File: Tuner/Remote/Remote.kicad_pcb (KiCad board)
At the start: 2 copper layers, 96.8 x 99.3 mm, 100 parts, among them J1 Conn_01x05, J10 Conn_01x05, J11 Conn_01x04, J12 Conn_01x04, J13 Conn_01x01, J14 Conn_01x01, J15 Conn_01x02, J16 Conn_01x06, J17 Conn_01x02, J18 Conn_01x01, J19 Conn_01x01, J2 Conn_01x05, J20 Conn_01x01, J21 Conn_01x01, J22 Conn_01x01, J23 Conn_01x01, J24 Conn_01x02, J26 Conn_01x02, J27 Conn_01x02, J3 USB_B, J4 Conn_01x04, J5 Conn_01x20, J6 Conn_02x03_Odd_Even, J7 Conn_01x02, J8 Conn_01x06, J9 Conn_01x20, Q1 2N7000, Q2 2N7000, Q3 2N7000, Q4 2N7000, U1 LM1117-3.3, U2 STM32F103C8T6, U4 LM7805_TO220, Y1 8 MHz, Y2 Crystal

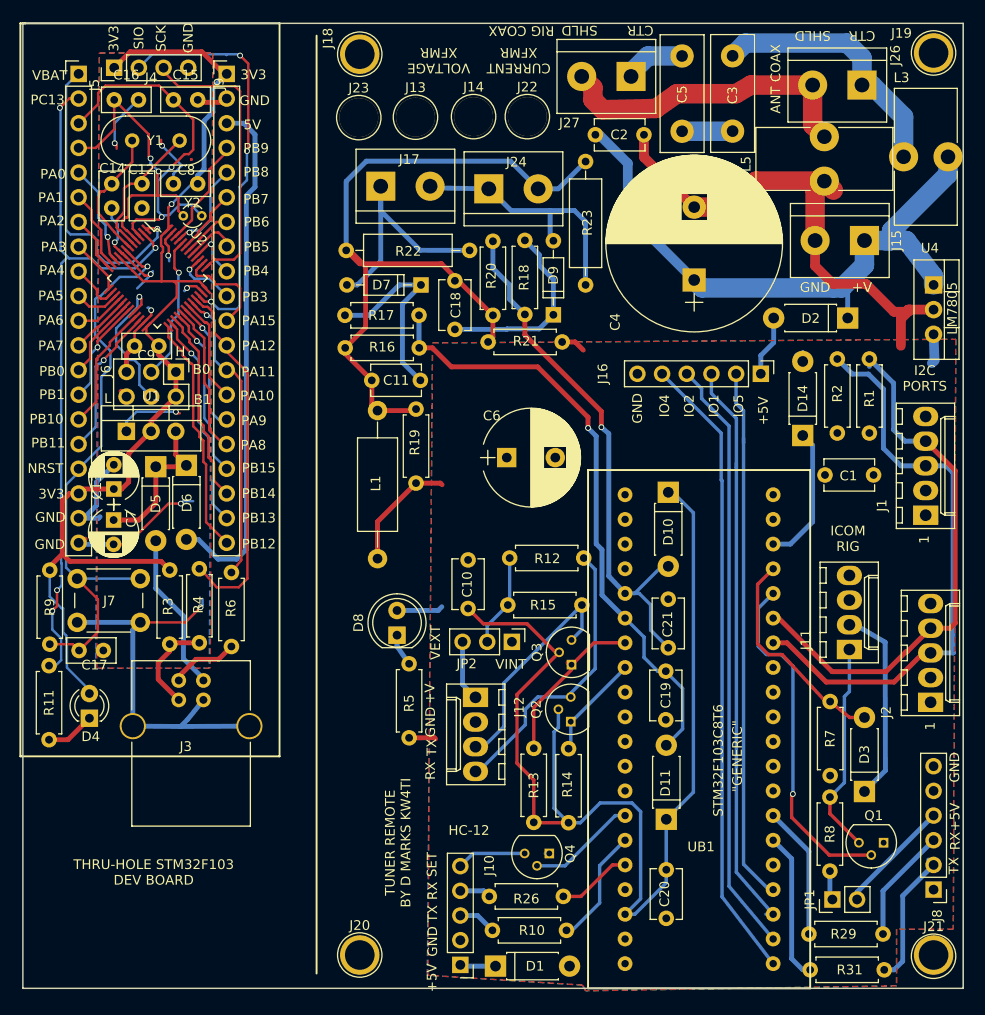
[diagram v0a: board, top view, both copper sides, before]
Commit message: JLCPCB order 09232018 - improved grounding - improved I2C cabling - NEO7M port - support for common mode chokes - relay board now has capacitors on all coils
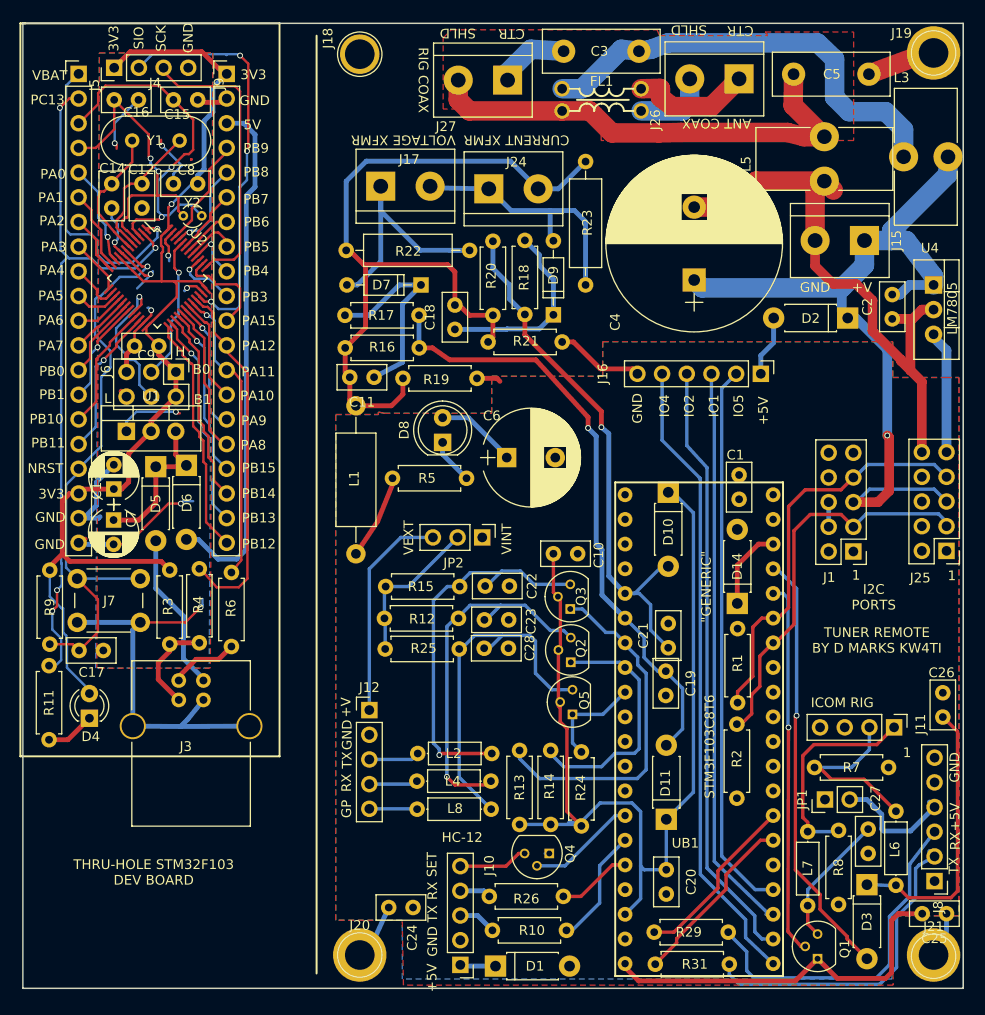
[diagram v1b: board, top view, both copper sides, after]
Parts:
- removed J13, J14, J22, J23: Conn_01x01, Connectors:1pin
- removed J2: Conn_01x05, Connectors_Molex:Molex_KK-6410-05_05x2.54mm_Straight
- added C22: 0.1 uF, Capacitors_THT:C_Disc_D5.0mm_W2.5mm_P2.50mm, F.Cu at (102.9, 86.9)
- added C23: 0.1 uF, Capacitors_THT:C_Disc_D5.0mm_W2.5mm_P2.50mm, F.Cu at (102.9, 90.3)
- added C24: 0.1 uF, Capacitors_THT:C_Disc_D5.0mm_W2.5mm_P2.50mm, F.Cu at (93.0, 120.0)
- added C25: 0.1 uF, Capacitors_THT:C_Disc_D5.0mm_W2.5mm_P2.50mm, F.Cu at (150.4, 120.6)
- added C26: 0.1 uF, Capacitors_THT:C_Disc_D5.0mm_W2.5mm_P2.50mm, F.Cu at (150.1, 97.9)
- added C27: 0.1 uF, Capacitors_THT:C_Disc_D5.0mm_W2.5mm_P2.50mm, F.Cu at (142.4, 111.9)
- added C28: 0.1 uF, Capacitors_THT:C_Disc_D5.0mm_W2.5mm_P2.50mm, F.Cu at (102.8, 93.3)
- added FL1: EMI_Filter_CommonMode, Remote:GenericCMCL, F.Cu at (114.9, 38.2)
- added J25: Conn_02x05_Odd_Even, Pin_Headers:Pin_Header_Straight_2x05_Pitch2.54mm, F.Cu at (150.4, 83.2)
- added L2: 100 uH, Inductors_THT:L_Axial_L5.3mm_D2.2mm_P7.62mm_Horizontal_Vishay_IM-1, F.Cu at (96.0, 104.1)
- added L4: 100 uH, Inductors_THT:L_Axial_L5.3mm_D2.2mm_P7.62mm_Horizontal_Vishay_IM-1, F.Cu at (95.9, 106.9)
- added L6: 100 uH, Inductors_THT:L_Axial_L5.3mm_D2.2mm_P7.62mm_Horizontal_Vishay_IM-1, F.Cu at (145.2, 117.7)
- added L7: 100 uH, Inductors_THT:L_Axial_L5.3mm_D2.2mm_P7.62mm_Horizontal_Vishay_IM-1, F.Cu at (136.1, 119.8)
- added L8: 100 uH, Inductors_THT:L_Axial_L5.3mm_D2.2mm_P7.62mm_Horizontal_Vishay_IM-1, F.Cu at (95.9, 109.8)
- added Q5: 2N7000, TO_SOT_Packages_THT:TO-92_Molded_Narrow, F.Cu at (111.9, 100.1)
- added R24: 10k, Resistors_THT:R_Axial_DIN0207_L6.3mm_D2.5mm_P7.62mm_Horizontal, F.Cu at (112.9, 103.9)
- added R25: 10k, Resistors_THT:R_Axial_DIN0207_L6.3mm_D2.5mm_P7.62mm_Horizontal, F.Cu at (92.7, 93.3)
- C1, C10, C11, C18, C19, C2, C20, C21: footprint Capacitors_THT:C_Disc_D5.1mm_W3.2mm_P5.00mm -> Capacitors_THT:C_Disc_D5.0mm_W2.5mm_P2.50mm
- J1: value Conn_01x05 -> Conn_02x05_Odd_Even; footprint Connectors_Molex:Molex_KK-6410-05_05x2.54mm_Straight -> Pin_Headers:Pin_Header_Straight_2x05_Pitch2.54mm
- J11: footprint Connectors_Molex:Molex_KK-6410-04_04x2.54mm_Straight -> Pin_Headers:Pin_Header_Straight_1x04_Pitch2.54mm
- J12: value Conn_01x04 -> Conn_01x05; footprint Connectors_Molex:Molex_KK-6410-04_04x2.54mm_Straight -> Pin_Headers:Pin_Header_Straight_1x05_Pitch2.54mm
- R12, R13, R14, R15: value 1k -> 10k
- moved R2 39.0 mm to (128.9, 108.7)
- moved C2 31.8 mm to (144.8, 59.4), turned to 90 degrees
- moved R1 24.3 mm to (128.9, 91.3), turned to 270 degrees
- moved D8 20.4 mm to (98.6, 72.1)
- moved C5 20.1 mm to (142.4, 34.2), turned to 180 degrees
- moved R5 20.0 mm to (101.0, 75.8), turned to 180 degrees
- moved D14 18.6 mm to (128.9, 88.7)
- moved R31 16.0 mm to (128.1, 125.8)
- moved R29 15.9 mm to (128.0, 122.5)
- moved R12 14.3 mm to (100.2, 90.2)
- moved Q1 13.7 mm to (137.2, 125.2), turned to 90 degrees
- moved R15 12.7 mm to (100.3, 86.9)
- moved J27 12.7 mm to (105.3, 34.8)
- moved J26 12.7 mm to (129.1, 34.7)
- moved R19 12.5 mm to (102.1, 65.5), turned to 180 degrees
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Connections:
- C2 pad 2: Net-(C2-Pad2) -> UPWR
- C4 pad 1: Net-(C2-Pad2) -> UPWR
- C5 pad 1: Net-(C3-Pad2) -> Net-(C5-Pad1)
- D2 pad 1: Net-(C2-Pad2) -> UPWR
- D3 pad 1: Net-(D3-Pad1) -> Net-(C26-Pad2)
- J1 pad 4: I2CSDA -> GND
- J1 pad 5: (no net) -> UPWR
- J11 pad 2: Net-(D3-Pad1) -> Net-(J11-Pad2)
- J15 pad 1: Net-(C2-Pad2) -> UPWR
- J19 pad 1: (no net) -> Net-(C5-Pad1)
- J20 pad 1: (no net) -> Net-(C24-Pad1)
- J21 pad 1: (no net) -> Net-(C25-Pad1)
- J26 pad 1: Net-(C3-Pad1) -> Net-(FL1-Pad1)
- J26 pad 2: SHIELD -> Net-(FL1-Pad3)
- J27 pad 1: Net-(C5-Pad2) -> Net-(C3-Pad2)
- J27 pad 2: SHIELD -> Net-(C5-Pad2)
- L3 pad 2: Net-(C2-Pad2) -> UPWR
- L5 pad 1: SHIELD -> Net-(C5-Pad2)
- Q1 pad 3: Net-(J11-Pad1) -> Net-(C27-Pad1)
- Q2 pad 3: Net-(J12-Pad4) -> Net-(C23-Pad1)
- Q3 pad 3: Net-(J12-Pad3) -> Net-(C22-Pad1)
- R12 pad 1: Net-(J12-Pad4) -> Net-(C23-Pad1)
- R15 pad 1: Net-(J12-Pad3) -> Net-(C22-Pad1)
- R7 pad 2: Net-(D3-Pad2) -> Net-(J11-Pad2)
- U4 pad 1: Net-(C2-Pad2) -> UPWR
- UB1 pad 14: (no net) -> Net-(Q5-Pad1)
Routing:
- net UPWR: track 0.00 -> 86.5 mm, vias 0 -> 1
- net Net-(C2-Pad2): track 70.5 -> 0.00 mm
- net GND: track 72.8 -> 123.0 mm
- net Net-(C5-Pad2): track 7.92 -> 48.9 mm
- net Net-(C22-Pad1): track 0.00 -> 40.2 mm, vias 0 -> 1
- net Net-(C23-Pad1): track 0.00 -> 38.7 mm, vias 0 -> 1
- net Net-(C28-Pad1): track 0.00 -> 36.7 mm
- net SHIELD: track 32.8 -> 0.00 mm
- net Net-(C26-Pad2): track 0.00 -> 28.8 mm
- net Net-(J12-Pad4): track 31.6 -> 5.02 mm
- net Net-(J8-Pad3): track 11.8 -> 35.7 mm
- net Net-(D3-Pad2): track 22.6 -> 44.6 mm, vias 0 -> 1
- net Net-(D3-Pad1): track 21.3 -> 0.00 mm
- net I2CSCL: track 60.3 -> 41.0 mm
- net Net-(J8-Pad2): track 14.2 -> 33.4 mm
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- added copper zone on F.Cu, net Net-(C5-Pad2)
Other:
- board text added: "GP"

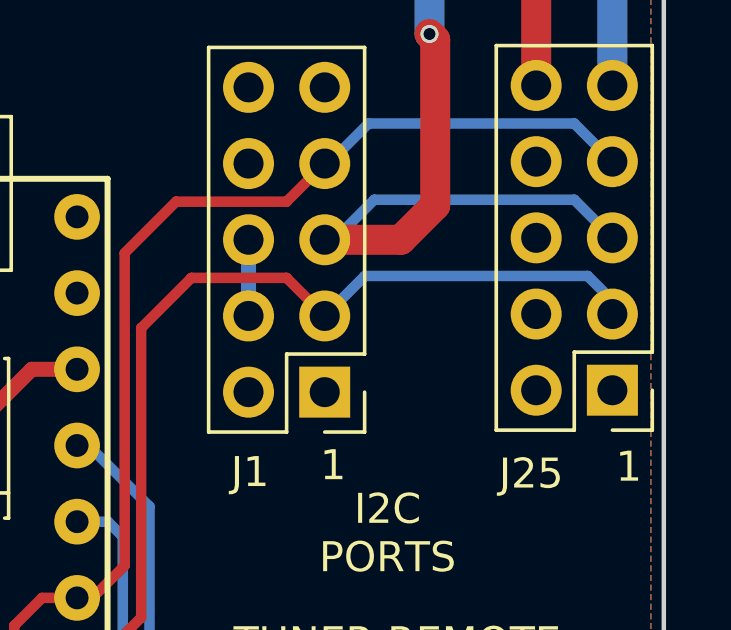
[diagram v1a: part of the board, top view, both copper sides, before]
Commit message: Changed I2C cable pinoutgit add Tunergit add Tuner Also added ICOM rig support
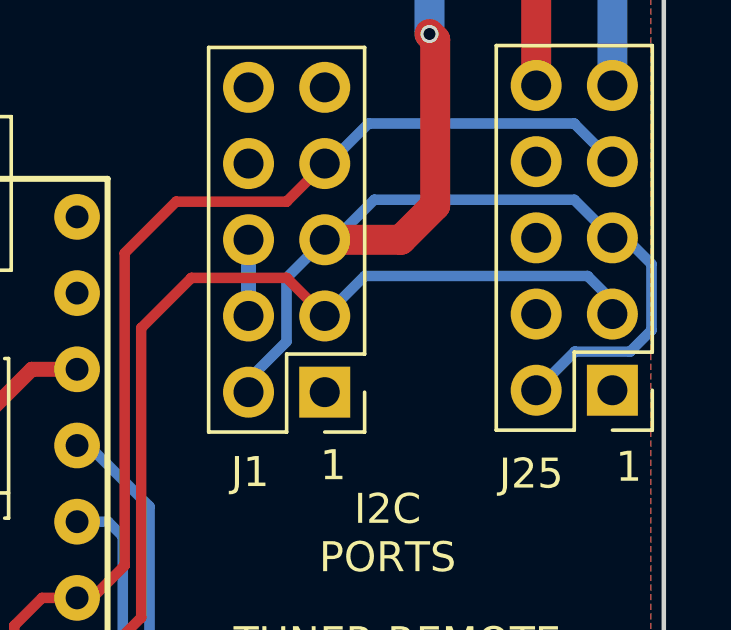
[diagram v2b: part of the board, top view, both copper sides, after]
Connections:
- J1 pad 2: +5V -> UPWR
- J25 pad 2: +5V -> UPWR
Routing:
- net UPWR: track 86.5 -> 101.2 mm
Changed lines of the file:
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@@
     (links 269)
     (no_connects 0)
-    (area 55.296999 28.880999 152.221001 128.345001)
+    (area 54.7794 27.3412 157.813882 129.469)
     (thickness 1.6)
     (drawings 103)
-    (tracks 1190)
+    (tracks 1200)
     (zones 0)
     (modules 112)
@@
   )
   (setup
-    (last_trace_width 0.25)
+    (last_trace_width 0.35)
     (user_trace_width 0.35)
     (user_trace_width 0.5)
@@
       (net 3 GND))
     (pad 2 thru_hole oval (at 2.54 0 180) (size 1.7 1.7) (drill 1) (layers *.Cu *.Mask)
-      (net 2 +5V))
+      (net 88 UPWR))
     (pad 3 thru_hole oval (at 0 2.54 180) (size 1.7 1.7) (drill 1) (layers *.Cu *.Mask)
       (net 8 I2CSCL))
@@
       (net 3 GND))
     (pad 2 thru_hole oval (at 2.54 0 180) (size 1.7 1.7) (drill 1) (layers *.Cu *.Mask)
-      (net 2 +5V))
+      (net 88 UPWR))
     (pad 3 thru_hole oval (at 0 2.54 180) (size 1.7 1.7) (drill 1) (layers *.Cu *.Mask)
       (net 8 I2CSCL))
@@
   (segment (start 108.5215 53.8734) (end 108.5215 52.7812) (width 0.5) (layer B.Cu) (net 87))
   (segment (start 109.9693 55.3212) (end 108.5215 53.8734) (width 0.5) (layer B.Cu) (net 87))
+  (segment (start 150.4315 78.1685) (end 150.8633 78.1685) (width 0.35) (layer B.Cu) (net 88))
+  (segment (start 150.8633 78.1685) (end 151.73452 79.03972) (width 0.35) (layer B.Cu) (net 88))
+  (segment (start 149.17928 81.96072) (end 147.8915 83.2485) (width 0.35) (layer B.Cu) (net 88))
+  (segment (start 151.02332 81.96072) (end 149.17928 81.96072) (width 0.35) (layer B.Cu) (net 88))
+  (segment (start 151.73452 81.24952) (end 151.02332 81.96072) (width 0.35) (layer B.Cu) (net 88))
+  (segment (start 151.73452 79.03972) (end 151.73452 81.24952) (width 0.35) (layer B.Cu) (net 88))
+  (segment (start 138.303 83.312) (end 138.303 82.89544) (width 0.35) (layer B.Cu) (net 88))
+  (segment (start 138.303 82.89544) (end 139.56792 81.63052) (width 0.35) (layer B.Cu) (net 88))
+  (segment (start 139.56792 81.63052) (end 139.56792 79.50708) (width 0.35) (layer B.Cu) (net 88))
+  (segment (start 139.56792 79.50708) (end 140.843 78.232) (width 0.35) (layer B.Cu) (net 88))
   (segment (start 139.6492 56.1848) (end 139.6492 58.674) (width 1) (layer B.Cu) (net 88) (status 20))
   (segment (start 139.6492 58.674) (end 140.2588 59.2836) (width 1) (layer B.Cu) (net 88) (status 30))
